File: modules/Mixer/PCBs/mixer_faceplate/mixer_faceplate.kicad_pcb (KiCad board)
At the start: 2 copper layers, 40.2 x 128.5 mm, 0 parts

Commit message: move mixer to active modules
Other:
- outline, holes or cut-outs redrawn

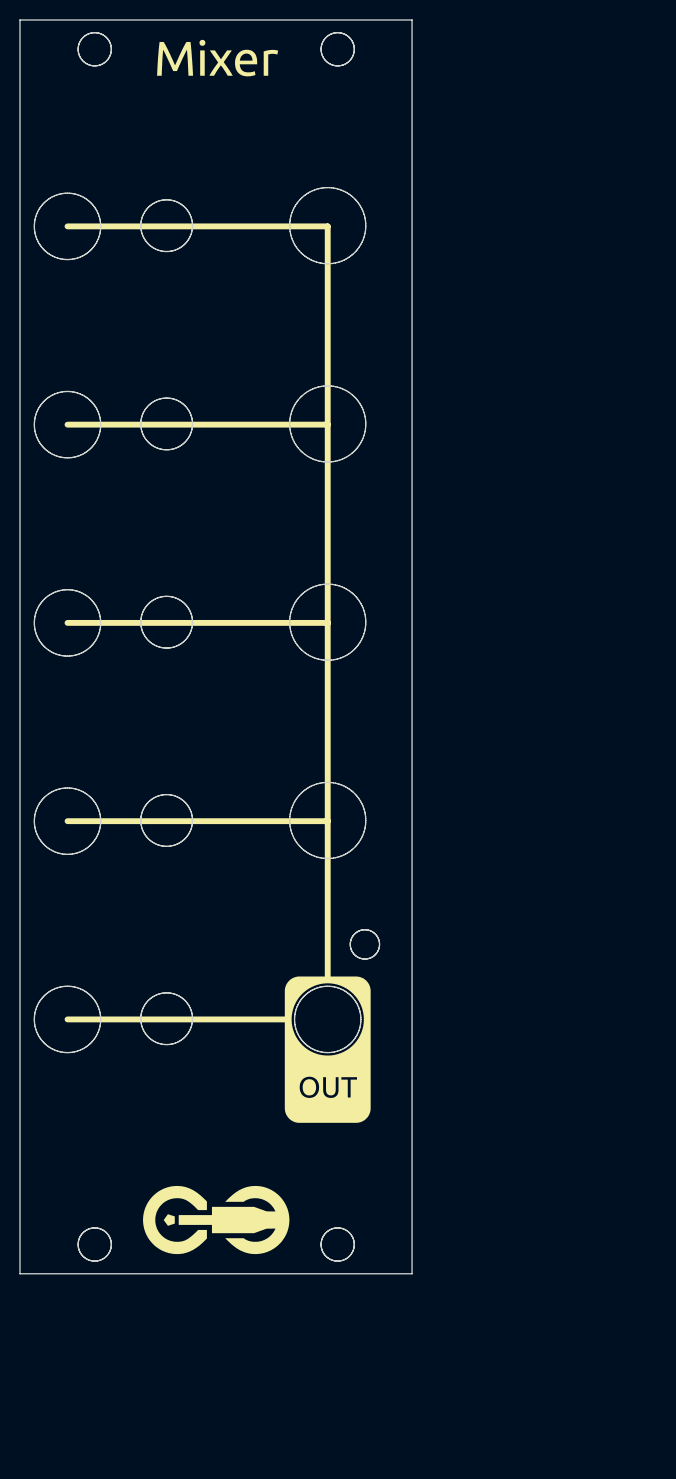
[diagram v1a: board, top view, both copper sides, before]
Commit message: regenerate mixer faceplate
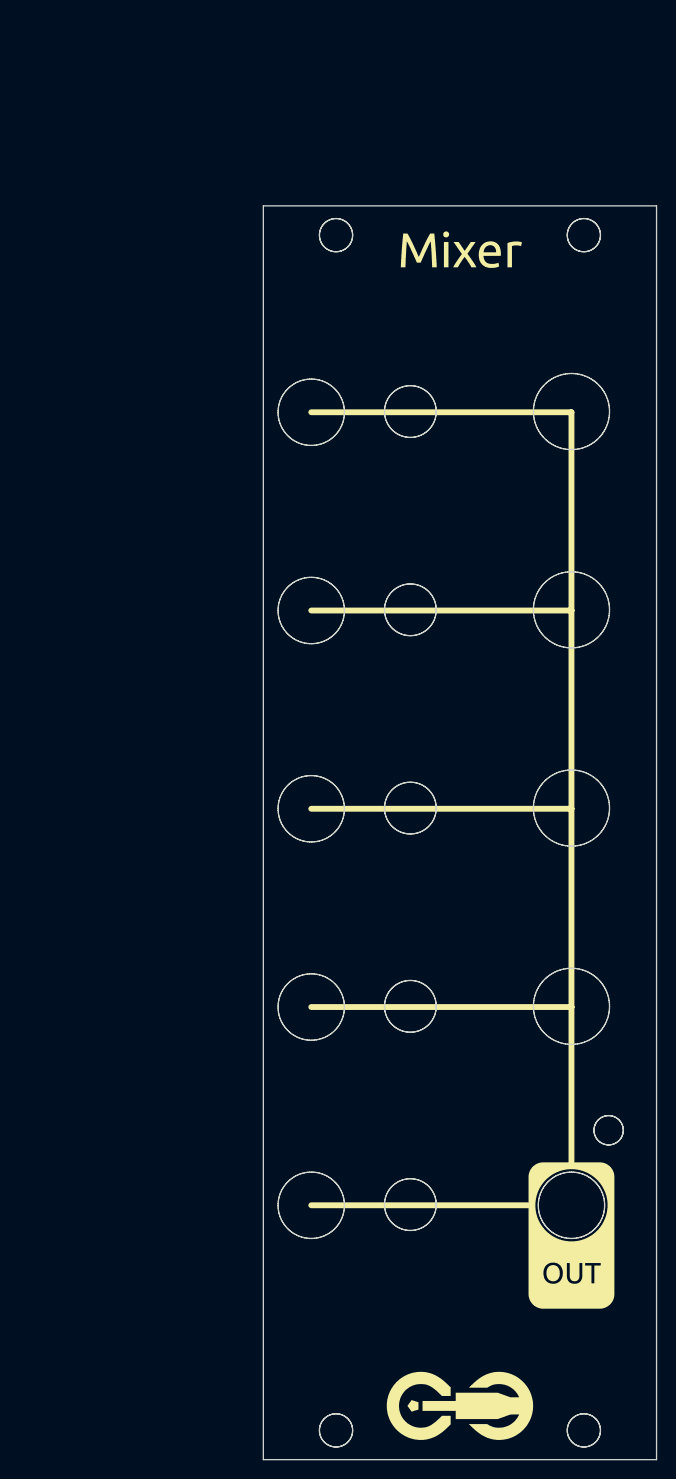
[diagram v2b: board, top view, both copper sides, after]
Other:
- board size 40.2 x 128.5 mm -> 40.3 x 128.5 mm
